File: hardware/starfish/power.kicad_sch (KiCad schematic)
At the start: 17 parts, among them U1 VX7805-500, U2 MIC5317-3.3

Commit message: First pass at schematic for starfish
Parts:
- removed C5: 100u, Capacitor_SMD:CP_Elec_6.3x7.7, symbol Device:C_Polarized_Small_US
- removed C8, C9: 100n, Capacitor_SMD:C_0402_1005Metric_Pad0.74x0.62mm_HandSolder, symbol Device:C_Small
- removed FB1, FB14: 50Ω @ 100MHz, Inductor_SMD:L_0603_1608Metric_Pad1.05x0.95mm_HandSolder, symbol Device:FerriteBead_Small
- removed RV1: 35V, Resistor_SMD:R_0603_1608Metric_Pad0.98x0.95mm_HandSolder, symbol Device:Varistor
- added C201, C202: 100n, symbol Device:C_Small
- added C203, C204, C205: 100u, Capacitor_SMD:CP_Elec_6.3x9.9, symbol Device:C_Polarized_Small_US
- added D201: TVS, symbol Device:D_Zener_Filled
- added D202: 20V, symbol Device:D_Zener_Filled
- added D203: 24V, winterbloom:LED_0805_Kingbright_APT2012, symbol Device:LED_Filled
- added D204, D205: 5V, winterbloom:LED_0805_Kingbright_APT2012, symbol Device:LED_Filled
- added F201: Fuse, Fuse:Fuseholder_Blade_Mini_Keystone_3568, symbol Device:Fuse
- added FB201: 60R @ 100MHz, symbol Device:FerriteBead_Small
- added J201: DC IN, winterbloom:TerminalBlock_CUI_TB002-500_1x02_P5.00mm_Vertical, symbol Connector:Screw_Terminal_01x02
- added J202: DC THRU, winterbloom:TerminalBlock_CUI_TB002-500_1x02_P5.00mm_Vertical, symbol Connector:Screw_Terminal_01x02
- added Q201: DMP3037LSS-13, Package_SO:SOIC-8_3.9x4.9mm_P1.27mm, symbol Transistor_FET:IRF7404
- added R201: 100R, symbol Device:R_US
- added R202, R203, R204: 5.1k, winterbloom:R_0402_HandSolder, symbol Device:R_US
- renumbered C2 to C206, C3 to C207, C4 to C208, C6 to C209, C7 to C210, TP1 to TP201, TP2 to TP202, TP3 to TP203, TP4 to TP204, U1 to U201, U2 to U202
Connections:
- net VIN_FILTERED is gone; now on net +24V: C206.1, C207.1, U201.1 (Vin)
- net +24V: now also C202.1, C203.1, C204.1, C205.1, D203.2 (A), FB201.2
- net +3V3: now also D205.2 (A)
- net +5V: now also D204.2 (A)
- net GND: now also C201.2, C202.2, C203.2, C204.2, C205.2, D201.2 (A), D202.2 (A), J201.2 (Pin_2), J202.2 (Pin_2), R201.2, R202.2, R203.2, R204.2
- new net: C201.1, F201.2, FB201.1
- new net: D203.1 (K), R202.1
- new net: D202.1 (K), F201.1, Q201.1 (S), Q201.2 (S), Q201.3 (S)
- new net: Q201.4 (G), R201.1
- new net: D204.1 (K), R203.1
- new net: D205.1 (K), R204.1
- new net DCIN: D201.1 (K), J201.1 (Pin_1), J202.1 (Pin_1), Q201.5 (D), Q201.6 (D), Q201.7 (D), Q201.8 (D)
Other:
- note added: "Power input, fusing, polarity protection, filtering, bulk capacitance"
- note removed: "* Base board provides reverse polarity protection * Base board provides large fuse for VDC"
- note removed: "MOV, & bulk capacitance"
- note removed: "Motor supply filter"
- title: Jellyfish -> Starfish
- moved on the sheet: C206, C207, C208, C209, C210, TP201, TP202, TP203, TP204, U201, U202

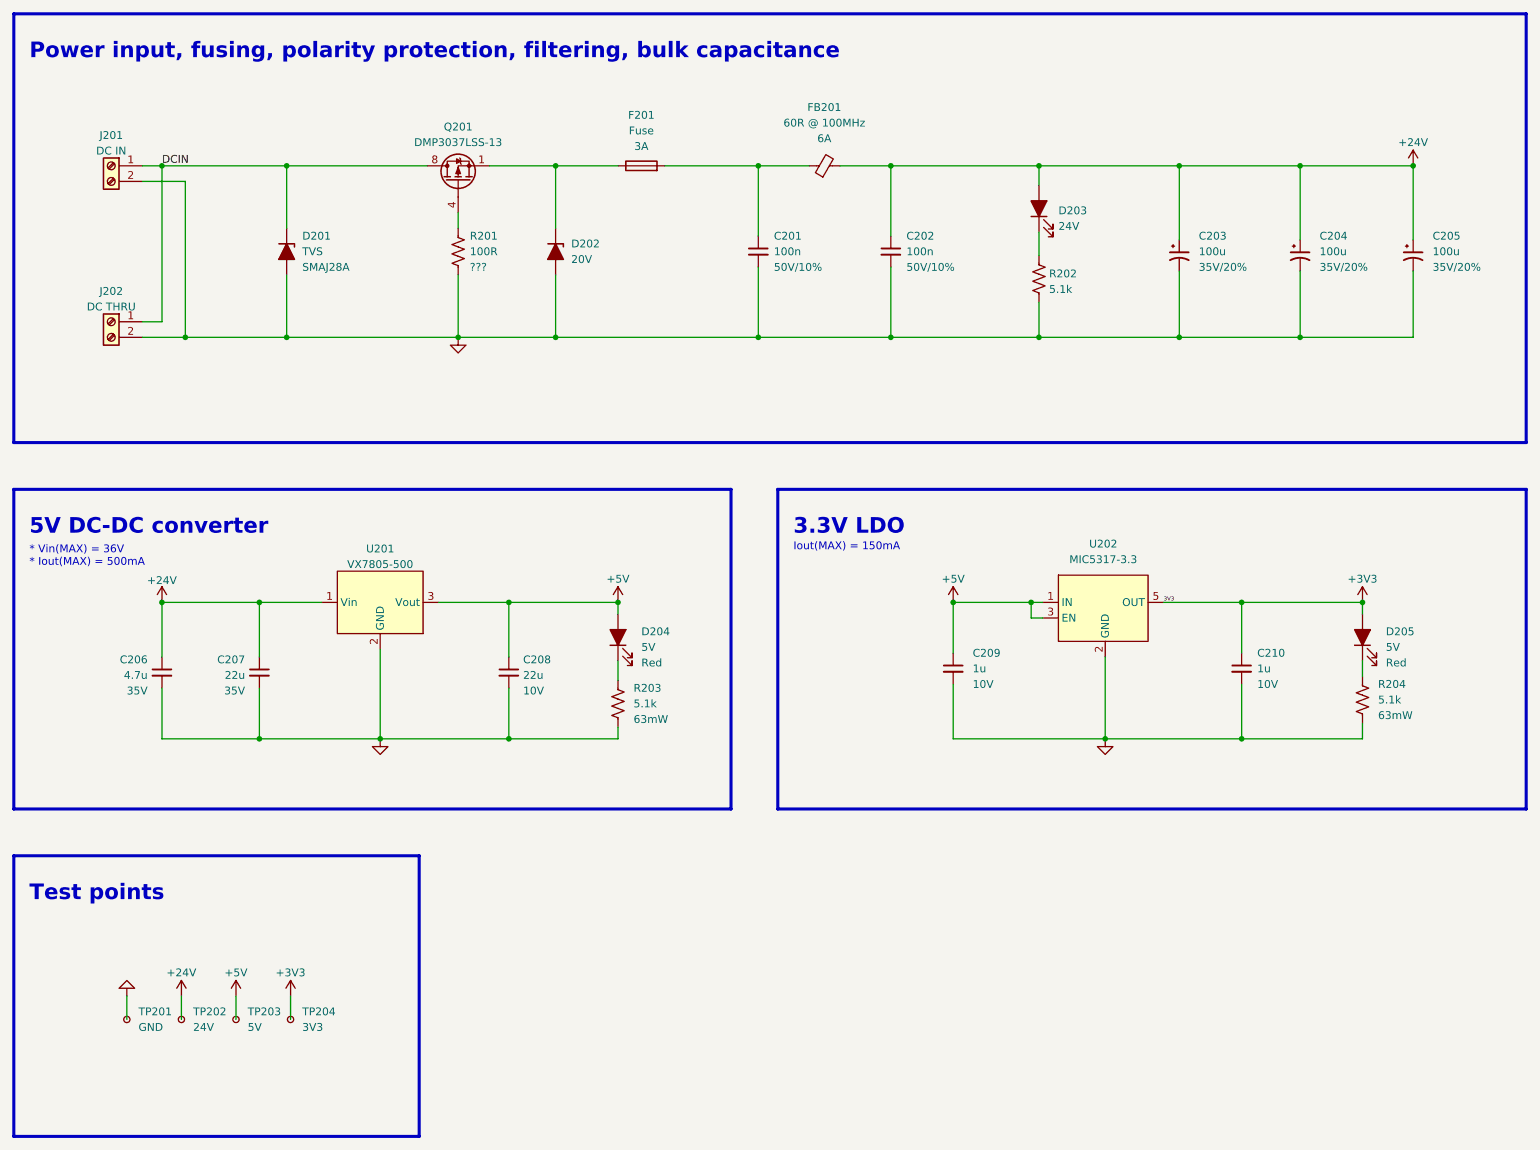
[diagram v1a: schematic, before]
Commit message: Mostly finished starfish schematic, ready for layout!
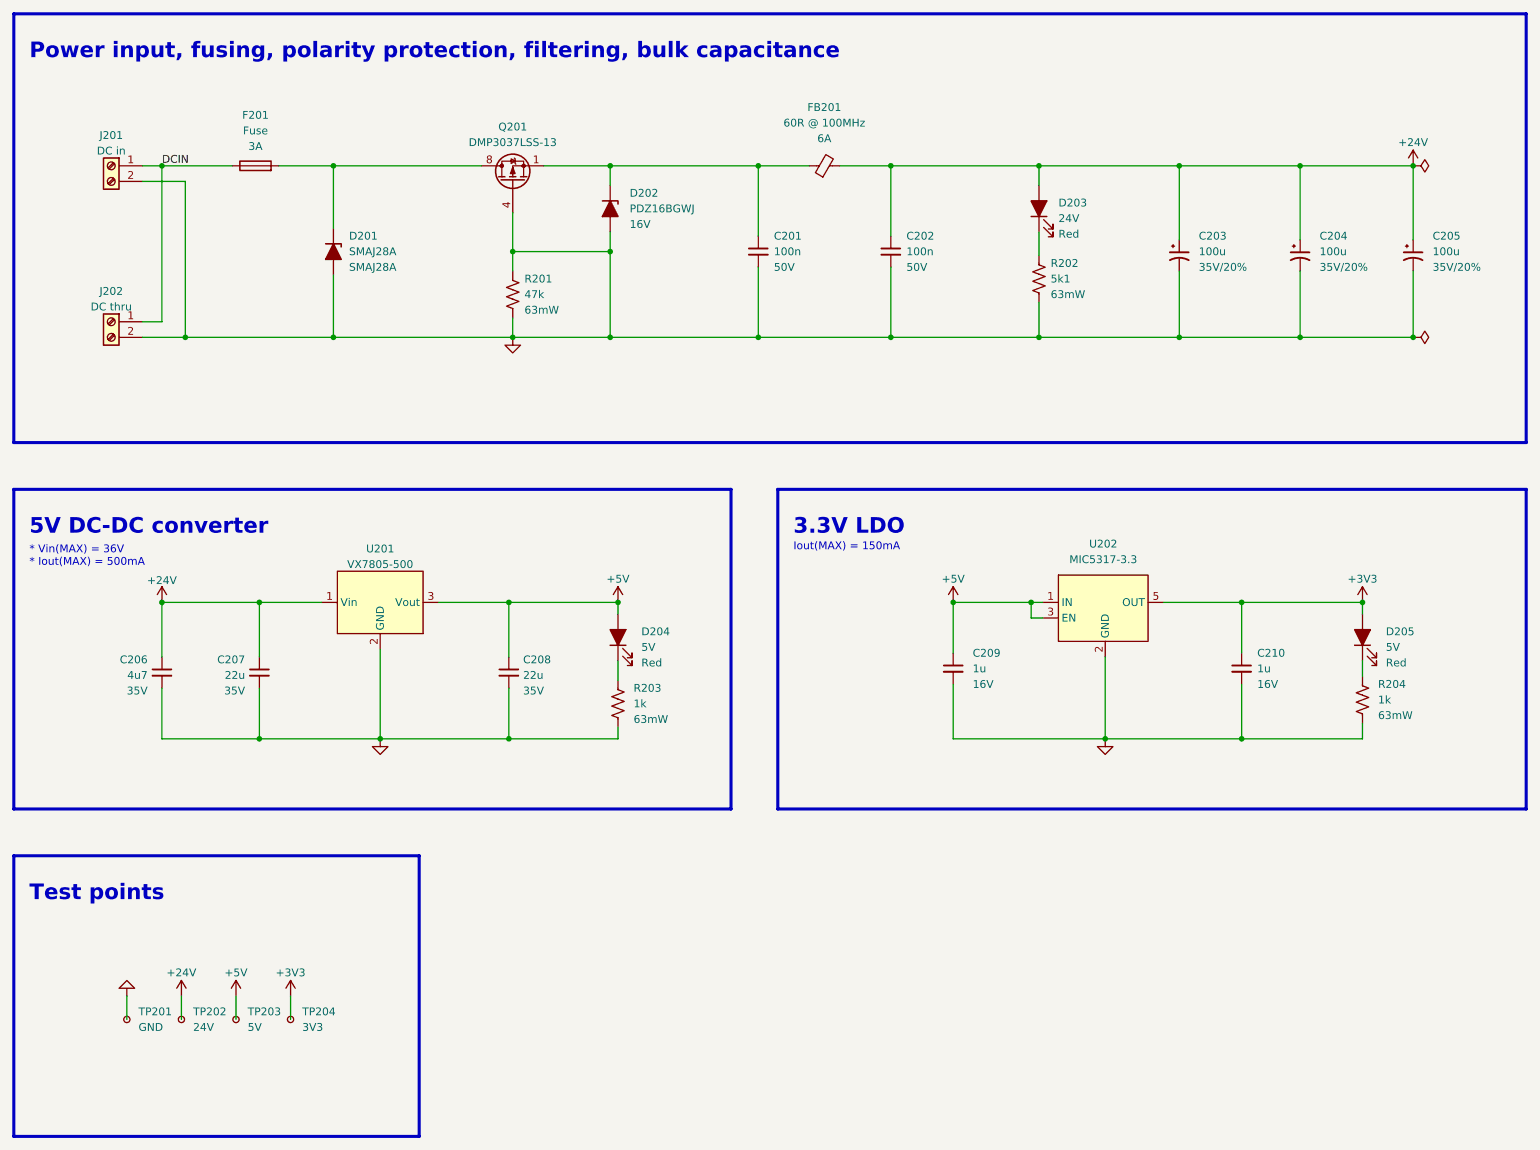
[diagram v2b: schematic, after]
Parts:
- C201, C202: footprint (none) -> winterbloom:C_0603_HandSolder; Rating 50V/10% -> 50V; mpn (none) -> CL10B104KB8NNWC
- C206: value 4.7u -> 4u7; footprint Capacitor_SMD:C_0805_2012Metric_Pad1.18x1.45mm_HandSolder -> winterbloom:C_0805_HandSolder; mpn ? -> (none)
- C207: footprint Capacitor_SMD:C_0805_2012Metric_Pad1.18x1.45mm_HandSolder -> winterbloom:C_0805_HandSolder
- C208: footprint Capacitor_SMD:C_0805_2012Metric_Pad1.18x1.45mm_HandSolder -> winterbloom:C_0805_HandSolder; Rating 10V -> 35V
- C209, C210: footprint Capacitor_SMD:C_0402_1005Metric_Pad0.74x0.62mm_HandSolder -> winterbloom:C_0402_HandSolder; Rating 10V -> 16V
- D201: value TVS -> SMAJ28A; footprint (none) -> Diode_SMD:D_SMA; Rating 30V+ -> 30V
- D202: value 20V -> PDZ16BGWJ; footprint (none) -> winterbloom:D_SOD-123; Rating (none) -> 16V; mpn (none) -> PDZ16BGWJ
- D203: Rating (none) -> Red
- F201: mpn (none) -> 3568
- FB201: footprint (none) -> Inductor_SMD:L_1806_4516Metric_Pad1.45x1.90mm_HandSolder
- J201: value DC IN -> DC in
- J202: value DC THRU -> DC thru
- Q201: mpn (none) -> DMP3037LSS-13
- R201: value 100R -> 47k; footprint (none) -> winterbloom:R_0402_HandSolder; Rating ??? -> 63mW
- R202: value 5.1k -> 5k1; Rating (none) -> 63mW
- R203, R204: value 5.1k -> 1k; mpn AC0603FR-075K1L -> RC0402JR-071KL
- TP201, TP202, TP203, TP204: mpn n/a -> (none)
- U201: mpn (none) -> VX7805-500
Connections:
- net DCIN: now also F201.1; no longer D201.1 (K), Q201.5 (D), Q201.6 (D), Q201.7 (D), Q201.8 (D)
- net GND: now also Q201.4 (G), R201.1
- net at C201.1, FB201.1: now also D202.1 (K), Q201.1 (S), Q201.2 (S), Q201.3 (S); no longer F201.2
- new net: D201.1 (K), F201.2, Q201.5 (D), Q201.6 (D), Q201.7 (D), Q201.8 (D)
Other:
- moved on the sheet: D201, D202, F201, Q201, R201

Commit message: First pass at layout and routing
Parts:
- removed C204, C205: 100u, Capacitor_SMD:CP_Elec_6.3x9.9, symbol Device:C_Polarized_Small_US
- D205: value 5V -> 3V3
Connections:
- net GND: no longer D202.2 (A), Q201.4 (G), R201.1
- net post polarity: now reaches C201.1, D202.1 (K), FB201.1, Q201.1 (S), Q201.2 (S), Q201.3 (S)
- net post fuse: now reaches D201.1 (K), F201.2, Q201.5 (D), Q201.6 (D), Q201.7 (D), Q201.8 (D)
- new net gate: D202.2 (A), Q201.4 (G), R201.1
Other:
- moved on the sheet: C201, C202, C203, C206, C207, D201, D202, D203, F201, FB201, J201, J202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

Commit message: Layout and routing mostly done! Just gotta make it prettier!
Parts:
- D201: footprint Diode_SMD:D_SMA -> winterbloom:D_SMA
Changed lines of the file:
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@@
       (effects (font (size 1.27 1.27)) (justify left))
     )
-    (property "Footprint" "Diode_SMD:D_SMA" (id 2) (at 92.71 55.245 0)
+    (property "Footprint" "winterbloom:D_SMA" (id 2) (at 92.71 55.245 0)
       (effects (font (size 1.27 1.27)) hide)
     )

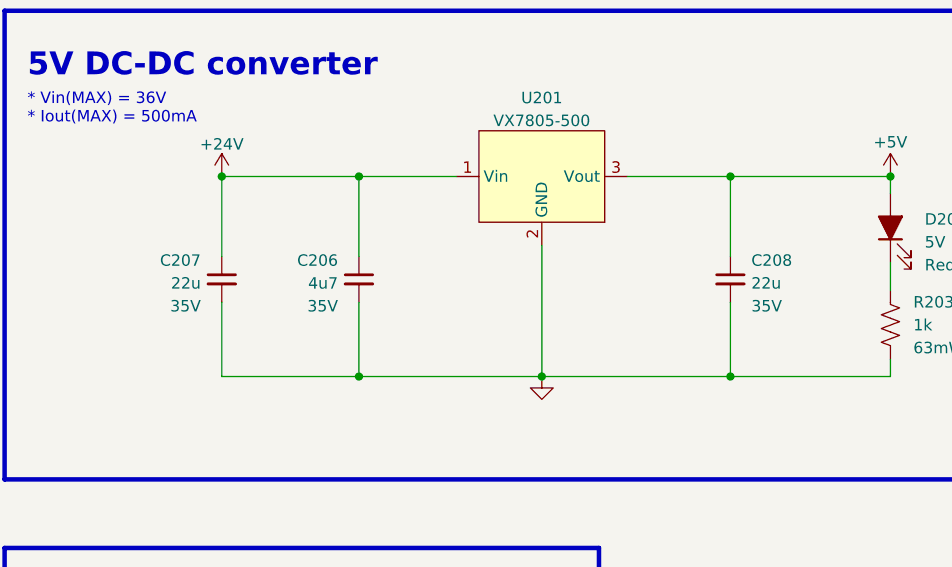
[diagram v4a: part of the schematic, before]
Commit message: Run through purchasing, update some cap sizes
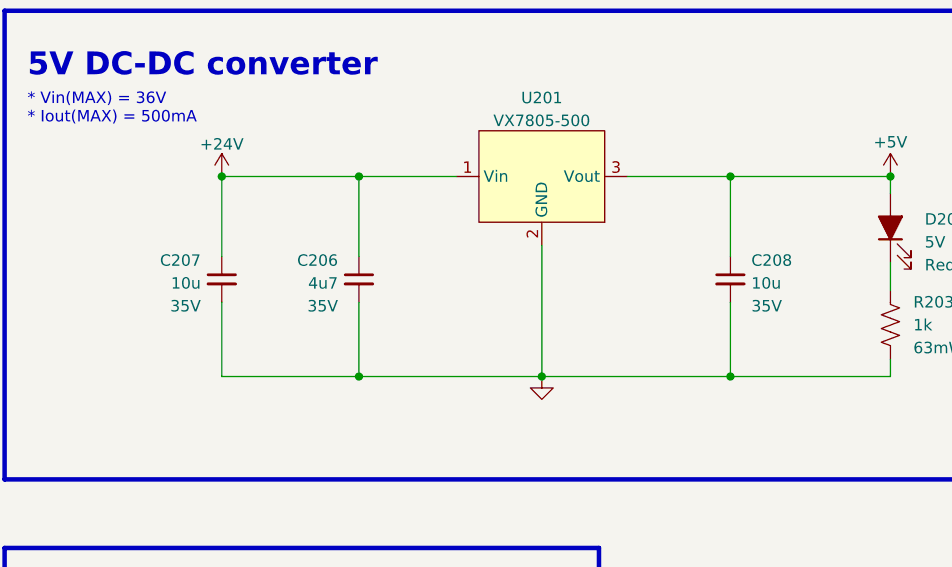
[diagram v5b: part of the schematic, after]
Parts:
- C203: mpn (none) -> 865080653016, UWT1V221MNL1GS
- C206: mpn (none) -> CL21A475KLCLQNC
- C207, C208: value 22u -> 10u; footprint winterbloom:C_0805_HandSolder -> winterbloom:C_1210_HandSolder; mpn C2012X5R1V226M125AC -> CL32A106KAULNNE
- R201: mpn (none) -> RC0402FR-0747KL
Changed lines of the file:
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@@
       (effects (font (size 1.27 1.27)) (justify left))
+    )
+    (property "mpn" "865080653016, UWT1V221MNL1GS" (id 5) (at 230.505 55.88 0)
+      (effects (font (size 1.27 1.27)) hide)
     )
     (pin "1")
@@
       (effects (font (size 1.27 1.27)) (justify left))
     )
-    (property "Value" "22u" (id 1) (at 99.4791 124.2651 0)
-      (effects (font (size 1.27 1.27)) (justify left))
-    )
-    (property "Footprint" "winterbloom:C_0805_HandSolder" (id 2) (at 97.155 123.825 0)
+    (property "Value" "10u" (id 1) (at 99.4791 124.2651 0)
+      (effects (font (size 1.27 1.27)) (justify left))
+    )
+    (property "Footprint" "winterbloom:C_1210_HandSolder" (id 2) (at 97.155 123.825 0)
       (effects (font (size 1.27 1.27)) hide)
     )
@@
       (effects (font (size 1.27 1.27)) hide)
     )
-    (property "mpn" "C2012X5R1V226M125AC" (id 4) (at 97.155 123.825 0)
+    (property "mpn" "CL32A106KAULNNE" (id 4) (at 97.155 123.825 0)
       (effects (font (size 1.27 1.27)) hide)
     )
@@
       (effects (font (size 1.27 1.27)) (justify right))
     )
-    (property "Value" "22u" (id 1) (at 38.316 124.2651 0)
-      (effects (font (size 1.27 1.27)) (justify right))
-    )
-    (property "Footprint" "winterbloom:C_0805_HandSolder" (id 2) (at 40.64 123.825 0)
+    (property "Value" "10u" (id 1) (at 38.316 124.2651 0)
+      (effects (font (size 1.27 1.27)) (justify right))
+    )
+    (property "Footprint" "winterbloom:C_1210_HandSolder" (id 2) (at 40.64 123.825 0)
       (effects (font (size 1.27 1.27)) hide)
     )
@@
       (effects (font (size 1.27 1.27)) hide)
     )
-    (property "mpn" "C2012X5R1V226M125AC" (id 4) (at 40.64 123.825 0)
+    (property "mpn" "CL32A106KAULNNE" (id 4) (at 40.64 123.825 0)
       (effects (font (size 1.27 1.27)) hide)
     )
@@
       (effects (font (size 1.27 1.27)) hide)
     )
-    (property "mpn" "" (id 4) (at 55.88 123.825 0)
+    (property "mpn" "CL21A475KLCLQNC" (id 4) (at 55.88 123.825 0)
       (effects (font (size 1.27 1.27)) hide)
     )
@@
       (effects (font (size 1.27 1.27)) (justify left))
     )
-    (pin "1")
+    (property "mpn" "RC0402FR-0747KL" (id 5) (at 121.92 62.23 0)
+      (effects (font (size 1.27 1.27)) hide)
+    )
+    (pin "1")
